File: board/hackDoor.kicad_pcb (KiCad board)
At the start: 2 copper layers, 63 x 34.5 mm, 11 parts, among them P1 RFID Reader, P2 Lock Button, P3 Lock/Unlock, P4 RFID Reader, P5 Lock Button, Q1 BSS138, SW1 SW_PUSH, U1 RFID-ID12

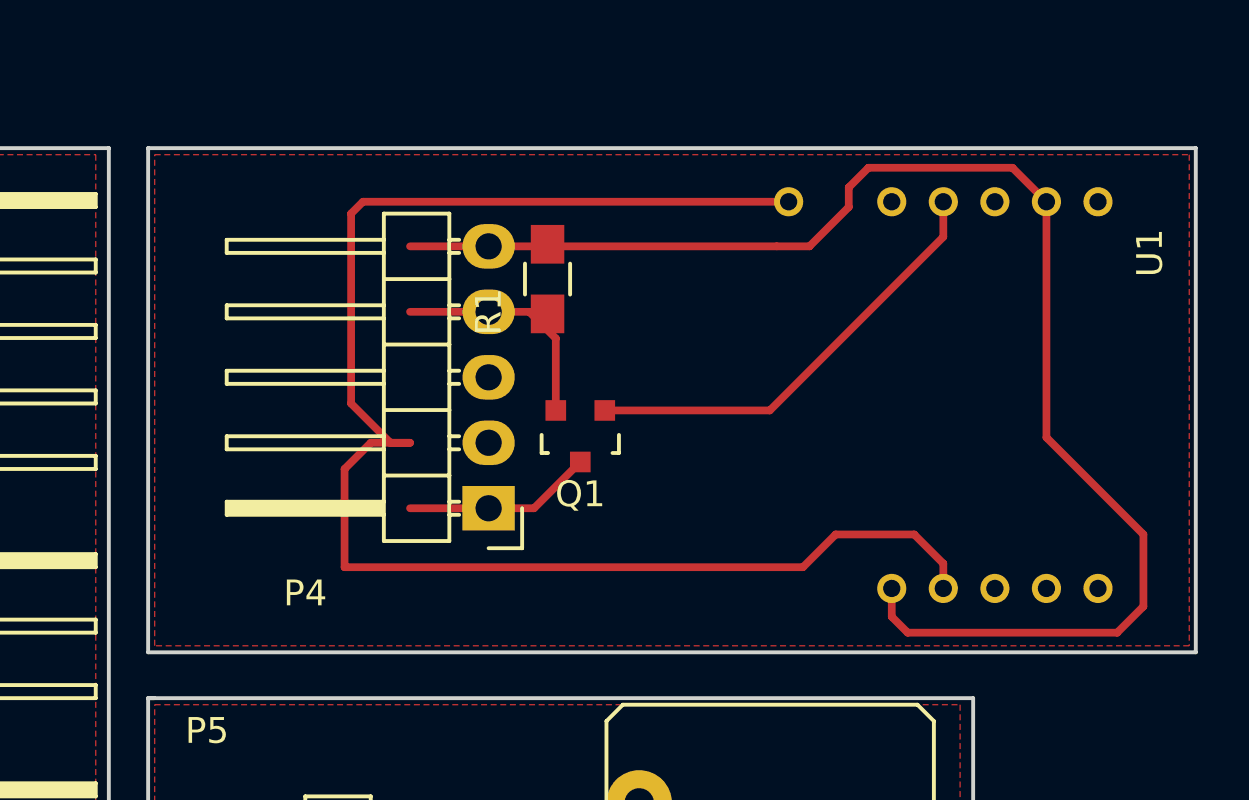
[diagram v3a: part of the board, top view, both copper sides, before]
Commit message: removed copper pour from under rfid module. detached copper pour on rfid reader board from ground net
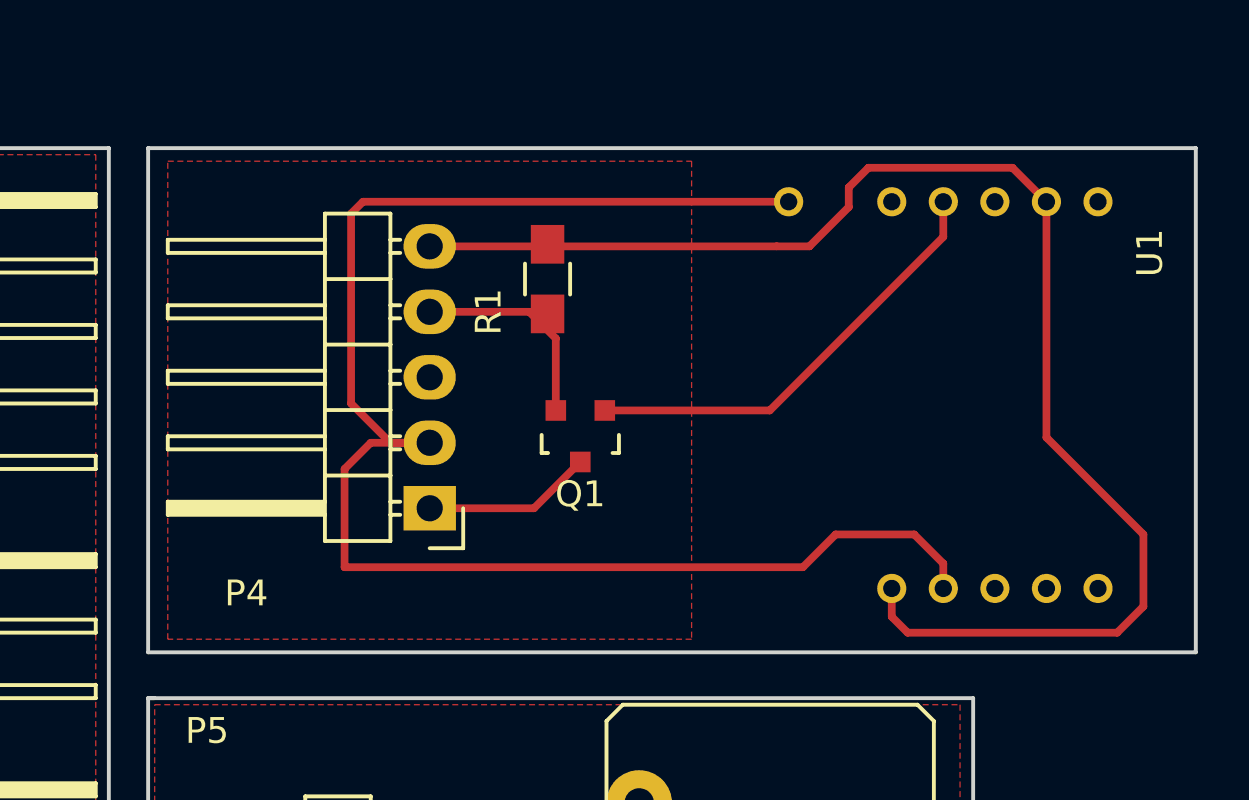
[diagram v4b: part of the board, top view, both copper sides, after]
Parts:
- moved P4 2.29 mm to (142.5, 105.4)
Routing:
- added copper zone on F.Cu, net (none)
- removed copper zone on F.Cu, net Net-(P4-Pad5)
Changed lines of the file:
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@@
   (general
     (links 26)
-    (no_connects 7)
-    (area 108.800862 87.247 175.335001 126.059001)
+    (no_connects 4)
+    (area 108.800862 87.247 172.287001 126.059001)
     (thickness 1.6)
     (drawings 14)
@@
     (last_trace_width 0.3)
     (trace_clearance 0.2)
-    (zone_clearance 0.508)
+    (zone_clearance 0.65)
     (zone_45_only no)
     (trace_min 0.2)
@@
   )
   (module Pin_Headers:Pin_Header_Angled_1x05 (layer F.Cu)
-    (at 144.78 105.41 180)
+    (at 142.494 105.41 180)
     (descr "Through hole pin header")
     (tags "pin header")
@@
     )
   )
-  (zone (net 12) (net_name "Net-(P4-Pad5)") (layer F.Cu) (hatch edge 0.508)
-    (connect_pads (clearance 0.508))
-    (min_thickness 0.254)
-    (fill yes (arc_segments 16) (thermal_gap 0.508) (thermal_bridge_width 0.508))
-    (polygon
-      (pts
-        (xy 171.958 110.744) (xy 131.826 110.744) (xy 131.826 91.694) (xy 171.958 91.694) (xy 171.958 110.744)
-      )
-    )
-  )
   (zone (net 15) (net_name "Net-(P5-Pad3)") (layer F.Cu) (hatch edge 0.508)
     (connect_pads (clearance 0.508))
@@
       )
     )
+  )
+  (zone (net 0) (net_name "") (layer F.Cu) (hatch edge 0.508)
+    (connect_pads (clearance 0.65))
+    (min_thickness 0.254)
+    (fill yes (arc_segments 16) (thermal_gap 0.508) (thermal_bridge_width 0.508))
+    (polygon
+      (pts
+        (xy 152.654 110.49) (xy 132.334 110.49) (xy 132.334 91.948) (xy 152.654 91.948) (xy 152.654 110.49)
+      )
+    )

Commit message: routing change
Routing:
- net Net-(P4-Pad5): track 55.7 -> 44.4 mm
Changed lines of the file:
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@@
     (thickness 1.6)
     (drawings 14)
-    (tracks 73)
+    (tracks 70)
     (zones 0)
     (modules 11)
@@
   (segment (start 146.356 97.79) (end 147.386 98.82) (width 0.3) (layer F.Cu) (net 11))
   (segment (start 147.386 101.61524) (end 147.386 98.82) (width 0.3) (layer F.Cu) (net 11))
+  (segment (start 160.418 108.52) (end 160.418 99.52) (width 0.3) (layer F.Cu) (net 12) (status 400000))
+  (segment (start 160.418 99.52) (end 166.418 93.52) (width 0.3) (layer F.Cu) (net 12) (status 800000))
   (segment (start 141.732 95.25) (end 146.986 95.25) (width 0.3) (layer F.Cu) (net 12))
   (segment (start 146.986 95.25) (end 155.956 95.25) (width 0.3) (layer F.Cu) (net 12))
@@
   (segment (start 159.512 92.202) (end 165.1 92.202) (width 0.3) (layer F.Cu) (net 12))
   (segment (start 165.1 92.202) (end 166.418 93.52) (width 0.3) (layer F.Cu) (net 12))
-  (segment (start 160.418 108.52) (end 160.418 109.618) (width 0.3) (layer F.Cu) (net 12))
-  (segment (start 166.418 102.664) (end 166.418 93.52) (width 0.3) (layer F.Cu) (net 12))
-  (segment (start 170.18 106.426) (end 166.418 102.664) (width 0.3) (layer F.Cu) (net 12))
-  (segment (start 170.18 109.22) (end 170.18 106.426) (width 0.3) (layer F.Cu) (net 12))
-  (segment (start 169.164 110.236) (end 170.18 109.22) (width 0.3) (layer F.Cu) (net 12))
-  (segment (start 161.036 110.236) (end 169.164 110.236) (width 0.3) (layer F.Cu) (net 12))
-  (segment (start 160.418 109.618) (end 161.036 110.236) (width 0.3) (layer F.Cu) (net 12))
   (segment (start 141.732 122.936) (end 146.224 122.936) (width 0.3) (layer F.Cu) (net 13))
   (segment (start 146.224 122.936) (end 146.558 123.27) (width 0.3) (layer F.Cu) (net 13))
@@
   (segment (start 155.68676 101.61524) (end 149.286 101.61524) (width 0.3) (layer F.Cu) (net 33))
   (segment (start 162.418 94.884) (end 155.68676 101.61524) (width 0.3) (layer F.Cu) (net 33))
+  (segment (start 162.415498 109.220391) (end 161.810909 109.984832) (width 0.3) (layer F.Cu) (net 34))
+  (segment (start 161.810909 109.984832) (end 160.280426 110.244411) (width 0.3) (layer F.Cu) (net 34))
+  (segment (start 162.415498 109.220391) (end 162.418 108.52) (width 0.3) (layer F.Cu) (net 34) (status 800000))
   (segment (start 141.732 102.87) (end 140.208 102.87) (width 0.3) (layer F.Cu) (net 34))
-  (segment (start 162.418 107.554) (end 162.418 108.52) (width 0.3) (layer F.Cu) (net 34))
-  (segment (start 161.29 106.426) (end 162.418 107.554) (width 0.3) (layer F.Cu) (net 34))
-  (segment (start 158.242 106.426) (end 161.29 106.426) (width 0.3) (layer F.Cu) (net 34))
-  (segment (start 156.972 107.696) (end 158.242 106.426) (width 0.3) (layer F.Cu) (net 34))
+  (segment (start 158.453346 109.595187) (end 160.280426 110.244411) (width 0.3) (layer F.Cu) (net 34))
+  (segment (start 156.972 107.696) (end 158.453346 109.595187) (width 0.3) (layer F.Cu) (net 34))
   (segment (start 139.192 107.696) (end 156.972 107.696) (width 0.3) (layer F.Cu) (net 34))
   (segment (start 139.192 103.886) (end 139.192 107.696) (width 0.3) (layer F.Cu) (net 34))
   (segment (start 140.208 102.87) (end 139.192 103.886) (width 0.3) (layer F.Cu) (net 34))
+  (segment (start 160.280426 110.244411) (end 160.280426 110.244411) (width 0.3) (layer F.Cu) (net 34))
   (segment (start 141.732 102.87) (end 140.97 102.87) (width 0.3) (layer F.Cu) (net 34))
   (segment (start 140.97 102.87) (end 139.446 101.346) (width 0.3) (layer F.Cu) (net 34))

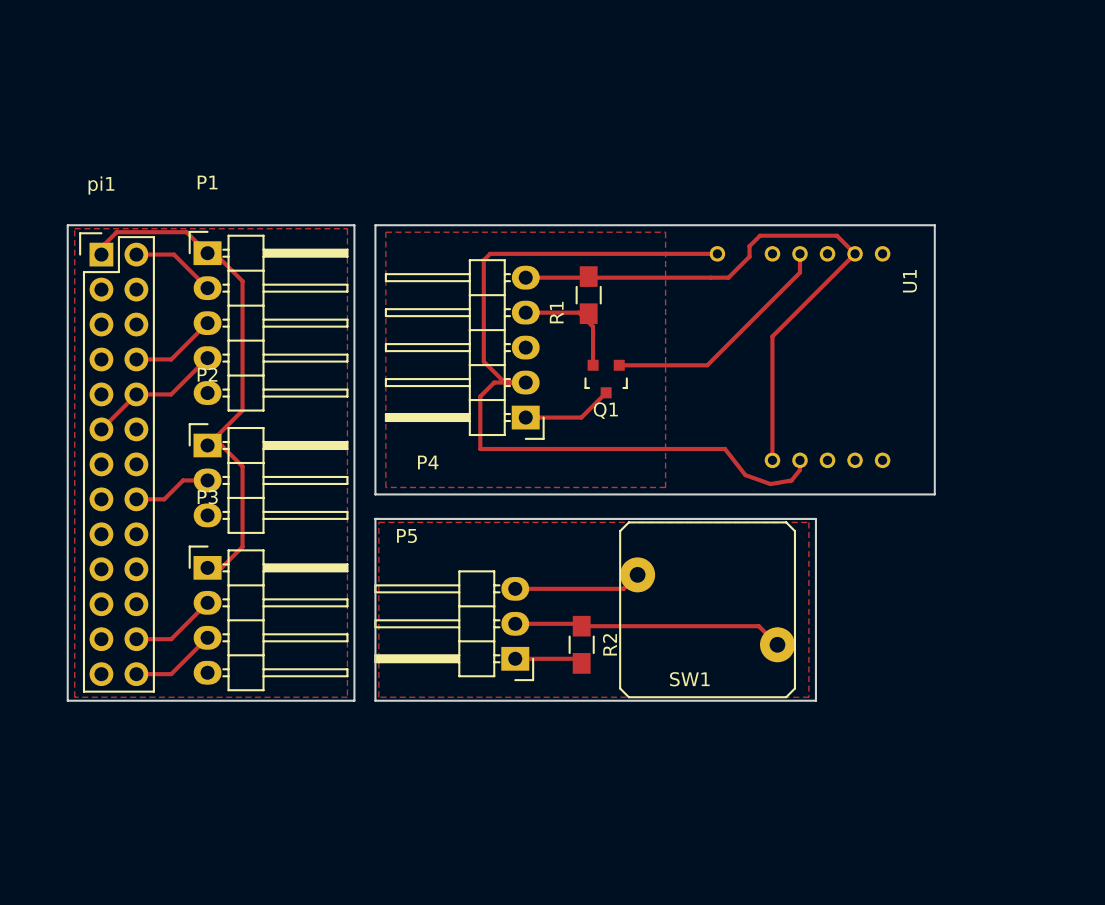
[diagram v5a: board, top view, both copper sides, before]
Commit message: added door and lock sensors. fixed the logic converter circuit on the rfid board
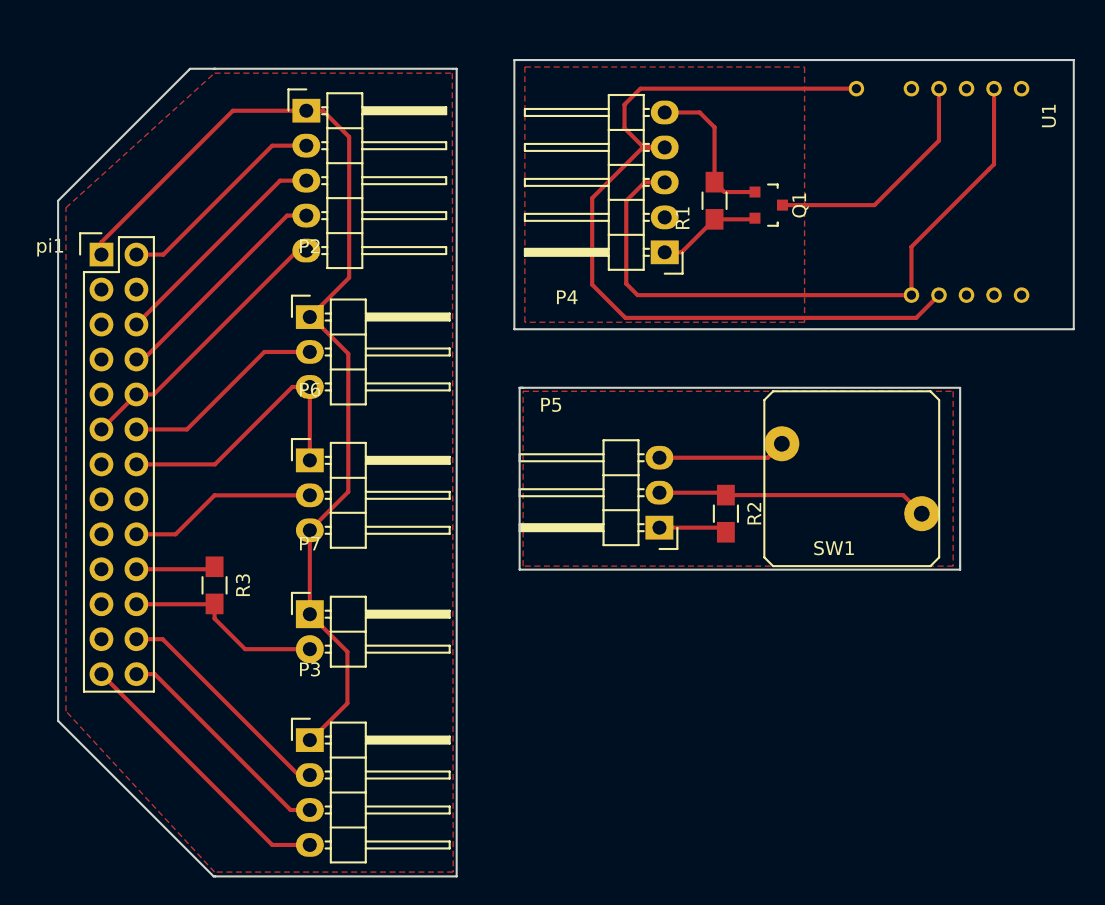
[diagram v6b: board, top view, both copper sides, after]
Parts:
- added P6: lockSensor, Pin_Headers:Pin_Header_Angled_1x03, F.Cu at (126.8, 108.5)
- added P7: doorSensor, Pin_Headers:Pin_Header_Angled_1x02, F.Cu at (126.8, 119.7)
- added R3: 1k, Resistors_SMD:R_0805_HandSoldering, F.Cu at (119.9, 117.6)
- moved Q1 17.3 mm to (160.1, 90.0), turned to 270 degrees
- moved P4 15.7 mm to (152.6, 93.4)
- moved U1 15.7 mm to (179.5, 84.5)
- moved P3 14.5 mm to (126.8, 128.8)
- moved R2 14.2 mm to (157.0, 112.4)
- moved P5 14.2 mm to (152.2, 113.4)
- moved SW1 14.2 mm to (166.2, 109.9)
- moved P1 12.6 mm to (126.6, 83.1)
- moved P2 11.9 mm to (126.8, 98.1)
- moved R1 11.4 mm to (156.2, 89.7)
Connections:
- P1 pad 4: /RX -> Net-(P1-Pad4)
- P1 pad 5: GND -> /RX
- P2 pad 3: GND -> Net-(P2-Pad3)
- P4 pad 1: /r3.3v -> Net-(P4-Pad1)
- P4 pad 5: Net-(P4-Pad5) -> /r3.3v
- Q1 pad 1: Net-(Q1-Pad1) -> /r3.3v
- Q1 pad 2: Net-(P4-Pad4) -> Net-(P4-Pad1)
- Q1 pad 3: /r3.3v -> Net-(Q1-Pad3)
- R1 pad 1: Net-(P4-Pad4) -> Net-(P4-Pad1)
- R1 pad 2: Net-(P4-Pad5) -> /r3.3v
- U1 pad 1: Net-(P4-Pad5) -> Net-(P4-Pad3)
- U1 pad 11: Net-(P4-Pad2) -> Net-(P4-Pad4)
- U1 pad 2: Net-(P4-Pad2) -> Net-(P4-Pad4)
- U1 pad 7: Net-(P4-Pad5) -> Net-(P4-Pad3)
- U1 pad 9: Net-(Q1-Pad1) -> Net-(Q1-Pad3)
- pi1 pad 12: Net-(pi1-Pad12) -> Net-(P2-Pad2)
- pi1 pad 14: Net-(pi1-Pad14) -> Net-(P2-Pad3)
- pi1 pad 16: Net-(P2-Pad2) -> Net-(pi1-Pad16)
- pi1 pad 25: Net-(pi1-Pad25) -> GND
- pi1 pad 6: GND -> Net-(P1-Pad3)
- pi1 pad 8: Net-(P1-Pad3) -> Net-(P1-Pad4)
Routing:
- net Net-(P4-Pad2): track 59.6 -> 0.00 mm
- net Net-(P4-Pad4): track 8.88 -> 62.5 mm
- net Net-(P4-Pad3): track 0.00 -> 47.9 mm
- net Net-(P4-Pad5): track 44.4 -> 0.00 mm
- net +3V3: track 38.7 -> 73.9 mm
- net Net-(P2-Pad3): track 0.00 -> 20.9 mm
- net GND: track 0.00 -> 20.3 mm
- net Net-(Q1-Pad1): track 17.3 -> 0.00 mm
- net Net-(Q1-Pad3): track 0.00 -> 17.1 mm
- net Net-(P1-Pad4): track 0.00 -> 16.7 mm
- net Net-(P7-Pad2): track 0.00 -> 15.2 mm
- net Net-(P6-Pad2): track 0.00 -> 13.8 mm
- net /RX: track 9.86 -> 21.0 mm
- net Net-(P3-Pad3): track 6.26 -> 16.7 mm
- net Net-(P3-Pad2): track 6.26 -> 16.7 mm
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- removed copper zone on F.Cu, net GND
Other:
- board size 63 x 34.5 mm -> 73.8 x 59.3 mm

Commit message: added mirrored fab outputs and increased pad diameter on rfid module
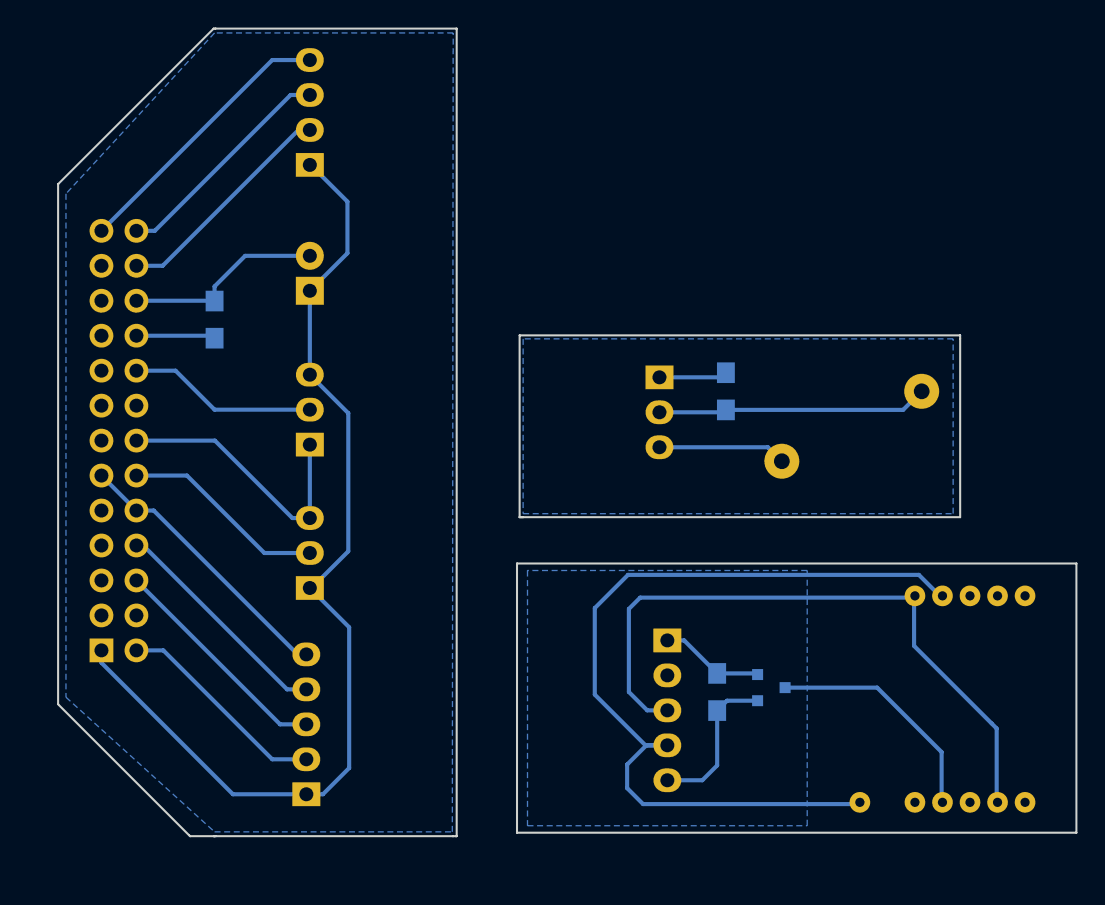
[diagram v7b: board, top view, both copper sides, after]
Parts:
- P1, P2, P3, P4, P5, P6, P7, Q1, R1, R2, R3, SW1, U1, pi1: moved to B.Cu
- moved P1 49.7 mm to (126.6, 132.8)
- moved U1 45.8 mm to (179.8, 130.4), turned to 90 degrees
- moved P3 41.8 mm to (126.8, 87.1)
- moved R1 35.7 mm to (156.4, 125.3), turned to 270 degrees
- moved Q1 35.1 mm to (160.3, 125.0), turned to 90 degrees
- moved pi1 28.8 mm to (111.7, 122.3)
- moved P4 28.2 mm to (152.8, 121.6)
- moved P7 23.5 mm to (126.8, 96.2)
- moved P2 19.7 mm to (126.8, 117.8)
- moved R3 19.3 mm to (119.9, 98.3), turned to 90 degrees
- moved P5 10.9 mm to (152.2, 102.5)
- moved R2 8.89 mm to (157.0, 103.5), turned to 90 degrees
- moved SW1 3.81 mm to (166.2, 106.0)
- moved P6 1.14 mm to (126.8, 107.4)
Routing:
- added copper zone on B.Cu, net (none)
- added copper zone on B.Cu, net GND
- added copper zone on B.Cu, net Net-(P5-Pad3)
- removed copper zone on F.Cu, net (none)
- removed copper zone on F.Cu, net Net-(P5-Pad3)
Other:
- board size 73.8 x 59.3 mm -> 74 x 58.7 mm
